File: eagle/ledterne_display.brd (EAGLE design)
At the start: 15 x 15 mm, 5 parts

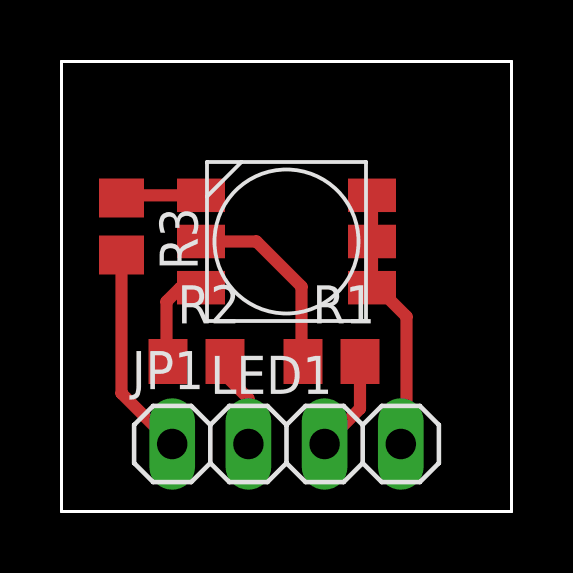
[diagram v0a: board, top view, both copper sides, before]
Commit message: Adjust placement of display board's connector
The connector is now placed in such way that, when connecting
the display board with the driver board by using a right-angle
pin header, the display board's borders are flush with the
driver board's borders.
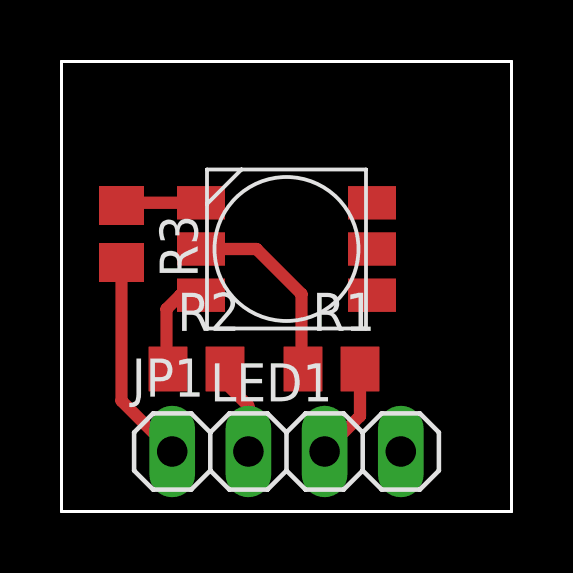
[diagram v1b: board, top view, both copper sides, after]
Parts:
- moved JP1 0.25 mm to (7.50, 2.00)
- moved LED1 0.25 mm to (7.50, 8.75)
- moved R1 0.25 mm to (9.00, 4.75)
- moved R2 0.25 mm to (4.50, 4.75)
- moved R3 0.25 mm to (2.00, 9.25)
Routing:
- net GND: track 8.96 -> 0.00 mm
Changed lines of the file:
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@@
 </autorouter>
 <elements>
-<element name="LED1" library="led-rgb" package="SMD_5252" value="RGB-5252" x="7.5" y="9"/>
-<element name="R1" library="resistor" package="R0805" value="" x="9" y="5"/>
-<element name="R2" library="resistor" package="R0805" value="" x="4.5" y="5"/>
-<element name="R3" library="resistor" package="R0805" value="" x="2" y="9.5" rot="R270"/>
-<element name="JP1" library="pinhead" package="1X04" value="" x="7.5" y="2.25"/>
+<element name="LED1" library="led-rgb" package="SMD_5252" value="RGB-5252" x="7.5" y="8.75"/>
+<element name="R1" library="resistor" package="R0805" value="" x="9" y="4.75"/>
+<element name="R2" library="resistor" package="R0805" value="" x="4.5" y="4.75"/>
+<element name="R3" library="resistor" package="R0805" value="" x="2" y="9.25" rot="R270"/>
+<element name="JP1" library="pinhead" package="1X04" value="" x="7.5" y="2"/>
 </elements>
 <signals>
@@
 <contactref element="R1" pad="1"/>
 <contactref element="LED1" pad="P2"/>
-<wire x1="4.65" y1="9" x2="6.5" y2="9" width="0.4064" layer="1"/>
-<wire x1="6.5" y1="9" x2="8" y2="7.5" width="0.4064" layer="1"/>
-<wire x1="8" y1="7.5" x2="8" y2="5.05" width="0.4064" layer="1"/>
-<wire x1="8" y1="5.05" x2="8.05" y2="5" width="0.4064" layer="1"/>
+<wire x1="4.65" y1="8.75" x2="6.5" y2="8.75" width="0.4064" layer="1"/>
+<wire x1="6.5" y1="8.75" x2="8" y2="7.25" width="0.4064" layer="1"/>
+<wire x1="8" y1="7.25" x2="8" y2="4.8" width="0.4064" layer="1"/>
+<wire x1="8" y1="4.8" x2="8.05" y2="4.75" width="0.4064" layer="1"/>
 </signal>
 <signal name="N$2">
 <contactref element="R2" pad="1"/>
 <contactref element="LED1" pad="P3"/>
-<wire x1="4.65" y1="7.46" x2="3.96" y2="7.46" width="0.4064" layer="1"/>
-<wire x1="3.96" y1="7.46" x2="3.5" y2="7" width="0.4064" layer="1"/>
-<wire x1="3.5" y1="7" x2="3.5" y2="5.05" width="0.4064" layer="1"/>
-<wire x1="3.5" y1="5.05" x2="3.55" y2="5" width="0.4064" layer="1"/>
+<wire x1="4.65" y1="7.21" x2="3.96" y2="7.21" width="0.4064" layer="1"/>
+<wire x1="3.96" y1="7.21" x2="3.5" y2="6.75" width="0.4064" layer="1"/>
+<wire x1="3.5" y1="6.75" x2="3.5" y2="4.8" width="0.4064" layer="1"/>
+<wire x1="3.5" y1="4.8" x2="3.55" y2="4.75" width="0.4064" layer="1"/>
 </signal>
 <signal name="N$3">
 <contactref element="R3" pad="1"/>
 <contactref element="LED1" pad="P1"/>
-<wire x1="4.65" y1="10.54" x2="2.09" y2="10.54" width="0.4064" layer="1"/>
-<wire x1="2.09" y1="10.54" x2="2" y2="10.45" width="0.4064" layer="1"/>
+<wire x1="4.65" y1="10.29" x2="2.09" y2="10.29" width="0.4064" layer="1"/>
+<wire x1="2.09" y1="10.29" x2="2" y2="10.2" width="0.4064" layer="1"/>
 </signal>
 <signal name="GND">
@@
 <contactref element="LED1" pad="P6"/>
 <contactref element="JP1" pad="4"/>
-<wire x1="10.35" y1="9" x2="10.35" y2="10.54" width="0.4064" layer="1"/>
-<wire x1="10.35" y1="7.46" x2="10.35" y2="9" width="0.4064" layer="1"/>
-<wire x1="10.35" y1="7.46" x2="10.54" y2="7.46" width="0.4064" layer="1"/>
-<wire x1="10.54" y1="7.46" x2="11.5" y2="6.5" width="0.4064" layer="1"/>
-<wire x1="11.5" y1="6.5" x2="11.5" y2="2.44" width="0.4064" layer="1"/>
-<wire x1="11.5" y1="2.44" x2="11.31" y2="2.25" width="0.4064" layer="1"/>
+<wire x1="10.35" y1="8.75" x2="10.35" y2="10.29" width="0" layer="19" extent="1-1"/>
+<wire x1="10.35" y1="7.21" x2="10.35" y2="8.75" width="0" layer="19" extent="1-1"/>
+<wire x1="11.31" y1="2" x2="10.35" y2="7.21" width="0" layer="19" extent="1-1"/>
 </signal>
 <signal name="LED_R">
 <contactref element="R1" pad="2"/>
 <contactref element="JP1" pad="3"/>
-<wire x1="9.95" y1="5" x2="9.95" y2="3.43" width="0.4064" layer="1"/>
-<wire x1="9.95" y1="3.43" x2="8.77" y2="2.25" width="0.4064" layer="1"/>
+<wire x1="9.95" y1="4.75" x2="9.95" y2="3.18" width="0.4064" layer="1"/>
+<wire x1="9.95" y1="3.18" x2="8.77" y2="2" width="0.4064" layer="1"/>
 </signal>
 <signal name="LED_G">
 <contactref element="JP1" pad="2"/>
 <contactref element="R2" pad="2"/>
-<wire x1="6.23" y1="2.25" x2="6.23" y2="3.77" width="0.4064" layer="1"/>
-<wire x1="6.23" y1="3.77" x2="5.5" y2="4.5" width="0.4064" layer="1"/>
-<wire x1="5.5" y1="4.5" x2="5.5" y2="4.95" width="0.4064" layer="1"/>
-<wire x1="5.5" y1="4.95" x2="5.45" y2="5" width="0.4064" layer="1"/>
+<wire x1="6.23" y1="2" x2="6.23" y2="3.52" width="0.4064" layer="1"/>
+<wire x1="6.23" y1="3.52" x2="5.5" y2="4.25" width="0.4064" layer="1"/>
+<wire x1="5.5" y1="4.25" x2="5.5" y2="4.7" width="0.4064" layer="1"/>
+<wire x1="5.5" y1="4.7" x2="5.45" y2="4.75" width="0.4064" layer="1"/>
 </signal>
 <signal name="LED_B">
 <contactref element="R3" pad="2"/>
 <contactref element="JP1" pad="1"/>
-<wire x1="2" y1="8.55" x2="2" y2="3.94" width="0.4064" layer="1"/>
-<wire x1="2" y1="3.94" x2="3.69" y2="2.25" width="0.4064" layer="1"/>
+<wire x1="2" y1="8.3" x2="2" y2="3.69" width="0.4064" layer="1"/>
+<wire x1="2" y1="3.69" x2="3.69" y2="2" width="0.4064" layer="1"/>
 </signal>
 </signals>

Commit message: Add ground plane on display board
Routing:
- added copper zone on layer 1, net GND
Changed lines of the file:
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@@
 <contactref element="LED1" pad="P6"/>
 <contactref element="JP1" pad="4"/>
-<wire x1="10.35" y1="8.75" x2="10.35" y2="10.29" width="0" layer="19" extent="1-1"/>
-<wire x1="10.35" y1="7.21" x2="10.35" y2="8.75" width="0" layer="19" extent="1-1"/>
-<wire x1="11.31" y1="2" x2="10.35" y2="7.21" width="0" layer="19" extent="1-1"/>
+<polygon width="0.4" layer="1" isolate="0.4" orphans="yes">
+<vertex x="0.5" y="0.5"/>
+<vertex x="14.5" y="0.5"/>
+<vertex x="14.5" y="14.5"/>
+<vertex x="0.5" y="14.5"/>
+</polygon>
 </signal>
 <signal name="LED_R">
